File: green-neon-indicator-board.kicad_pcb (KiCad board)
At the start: 2 copper layers, 20 x 20 mm, 3 parts

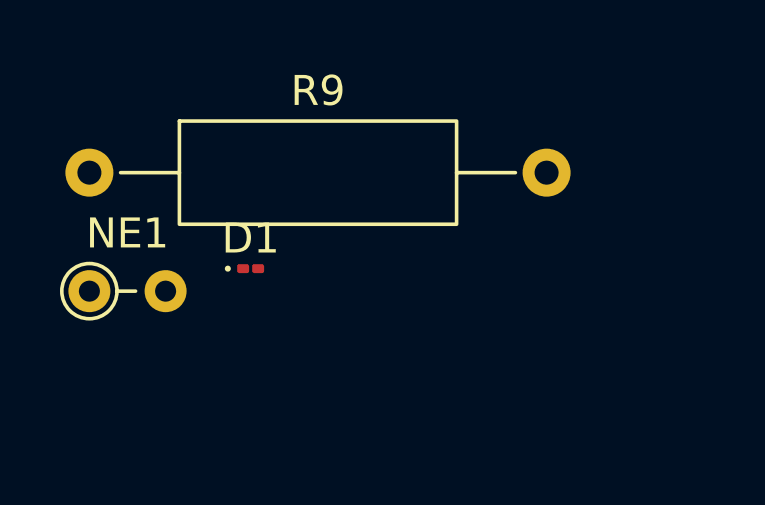
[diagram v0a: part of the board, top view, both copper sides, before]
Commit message: Select part numbers for enable control circuit
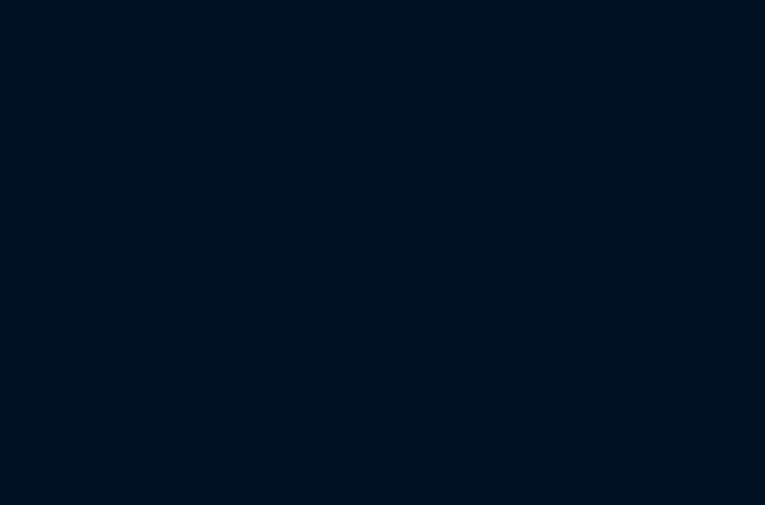
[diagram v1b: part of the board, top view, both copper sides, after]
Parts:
- removed D1: D_Schottky, Diode_SMD:D_01005_0402Metric
- removed NE1: Green Neon Lamp, Resistor_THT:R_Axial_DIN0204_L3.6mm_D1.6mm_P2.54mm_Vertical
- removed R9: 330k, Resistor_THT:R_Axial_DIN0309_L9.0mm_D3.2mm_P15.24mm_Horizontal

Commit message: Select all component values, initial layout and routing
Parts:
- added C1: 10u, Capacitor_SMD:C_0402_1005Metric_Pad0.74x0.62mm_HandSolder, F.Cu at (111.2, 108.0)
- added C2: 100n, Capacitor_SMD:C_0402_1005Metric_Pad0.74x0.62mm_HandSolder, F.Cu at (110.1, 108.0)
- added C3: 100n, Capacitor_SMD:C_0402_1005Metric_Pad0.74x0.62mm_HandSolder, F.Cu at (108.4, 109.7)
- added C4: 470n, Capacitor_SMD:C_0402_1005Metric_Pad0.74x0.62mm_HandSolder, F.Cu at (100.2, 110.9)
- added C5: 100n, Capacitor_SMD:C_1206_3216Metric_Pad1.33x1.80mm_HandSolder, F.Cu at (97.6, 91.2)
- added D1: US1G-E3/61T, Diode_SMD:D_SMA, F.Cu at (94.1, 94.4)
- added J1: 1x3 THT Headers, Connector_PinHeader_2.54mm:PinHeader_1x03_P2.54mm_Vertical, F.Cu at (103.4, 87.3)
- added J2: JST XH Compatible, Connector_JST:JST_XH_B3B-XH-A_1x03_P2.50mm_Vertical, F.Cu at (104.5, 97.7)
- added NE1: Green Neon Lamp, Resistor_THT:R_Axial_DIN0204_L3.6mm_D1.6mm_P2.54mm_Vertical, F.Cu at (91.5, 112.8)
- added Q1: IRLML0100TRPBF, Package_TO_SOT_SMD:SOT-23-3, F.Cu at (101.0, 108.5)
- added Q2: PJA138K, Package_TO_SOT_SMD:TSOT-23, F.Cu at (109.3, 104.0)
- added Q3: PJA138K, Package_TO_SOT_SMD:TSOT-23, F.Cu at (104.3, 104.0)
- added R10: 1M, Resistor_SMD:R_0402_1005Metric_Pad0.72x0.64mm_HandSolder, F.Cu at (97.6, 89.2)
- added R11: 330k, Resistor_THT:R_Axial_DIN0309_L9.0mm_D3.2mm_P15.24mm_Horizontal, F.Cu at (87.4, 91.0)
- added R12: 10k, Resistor_SMD:R_0402_1005Metric_Pad0.72x0.64mm_HandSolder, F.Cu at (112.7, 102.8)
- added R13: 100k, Resistor_SMD:R_0402_1005Metric_Pad0.72x0.64mm_HandSolder, F.Cu at (112.7, 104.0)
- added R3: 110k, Resistor_SMD:R_0402_1005Metric_Pad0.72x0.64mm_HandSolder, F.Cu at (108.4, 108.6)
- added R4: 10k, Resistor_SMD:R_0402_1005Metric_Pad0.72x0.64mm_HandSolder, F.Cu at (102.5, 110.9)
- added R5: 0.5, Resistor_SMD:R_0402_1005Metric_Pad0.72x0.64mm_HandSolder, F.Cu at (98.3, 110.2)
- added R6: 499k, Resistor_SMD:R_0402_1005Metric_Pad0.72x0.64mm_HandSolder, F.Cu at (108.4, 113.6)
- added R7: 499k, Resistor_SMD:R_0402_1005Metric_Pad0.72x0.64mm_HandSolder, F.Cu at (108.4, 112.5)
- added R8: 499k, Resistor_SMD:R_0402_1005Metric_Pad0.72x0.64mm_HandSolder, F.Cu at (106.1, 112.5)
- added R9: 10k, Resistor_SMD:R_0402_1005Metric_Pad0.72x0.64mm_HandSolder, F.Cu at (108.4, 110.7)
- added REF**: MountingHole_2.2mm_M2_DIN965, MountingHole:MountingHole_2.2mm_M2_DIN965, F.Cu at (112.7, 87.3)
- added REF**: MountingHole_2.2mm_M2_DIN965, MountingHole:MountingHole_2.2mm_M2_DIN965, F.Cu at (112.6, 112.7)
- added REF**: MountingHole_2.2mm_M2_DIN965, MountingHole:MountingHole_2.2mm_M2_DIN965, F.Cu at (87.2, 112.7)
- added REF**: MountingHole_2.2mm_M2_DIN965, MountingHole:MountingHole_2.2mm_M2_DIN965, F.Cu at (87.3, 87.3)
- added T1: WURTH_750311692, CustomLibraries:WURTH_750311692, F.Cu at (95.7, 101.4)
- added U1: ~, CustomLibraries:LM5155, F.Cu at (105.2, 109.3)
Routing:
- net +150V: track 0.00 -> 29.4 mm
- net /EN_INPUT: track 0.00 -> 18.7 mm
- net Net-(Q1-D): track 0.00 -> 8.66 mm
- net Net-(NE1-Pad1): track 0.00 -> 8.29 mm
- net /BOOST_EN: track 0.00 -> 8.21 mm, vias 0 -> 2
- net Net-(Q2-G): track 0.00 -> 7.00 mm
- net V_{BIAS}: track 0.00 -> 6.72 mm
- net Net-(Q1-S): track 0.00 -> 6.26 mm
- net Net-(Q1-G): track 0.00 -> 5.36 mm
- net Net-(U1-FB): track 0.00 -> 4.97 mm
- net Net-(U1-RT): track 0.00 -> 1.84 mm
- net Net-(U1-SS): track 0.00 -> 1.74 mm
- net Net-(U1-COMP): track 0.00 -> 1.30 mm
- net Net-(C4-Pad1): track 0.00 -> 1.14 mm
- net Net-(R7-Pad2): track 0.00 -> 1.11 mm
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- added copper zone on F.Cu, net +150V
- added copper zone on B.Cu, net GND
- added copper zone on F.Cu, net GND
- added copper zone on F.Cu, net Net-(D1-A)
- added copper zone on F.Cu, net Net-(T1-SB)
- added copper zone on F.Cu, net V_{BIAS}
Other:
- board size 20 x 20 mm -> 30 x 30 mm
- board text added: "Current Limiting Resistor"
- board text added: "ENABLE"
- board text added: "GND"
- board text added: "V_{IN}"

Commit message: Add lcsc part number to schematic symbols, prep design for manufacturing
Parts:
- C1: footprint Capacitor_SMD:C_0402_1005Metric_Pad0.74x0.62mm_HandSolder -> Capacitor_SMD:C_0603_1608Metric_Pad1.08x0.95mm_HandSolder
- NE1: footprint Resistor_THT:R_Axial_DIN0204_L3.6mm_D1.6mm_P2.54mm_Vertical -> Connector_PinHeader_2.54mm:PinHeader_1x02_P2.54mm_Vertical
- moved C1 0.40 mm to (111.6, 108.0)
- turned NE1 to 90 degrees
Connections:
- net Net-(Q1-S) renamed /CS
- net Net-(U1-FB) renamed /FB
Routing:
- net GND: vias 53 -> 21
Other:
- board text added: "Neon Bulb"
